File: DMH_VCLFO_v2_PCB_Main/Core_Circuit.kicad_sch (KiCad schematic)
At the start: 70 parts, among them J12 Conn_02x06_Top_Bottom, J13 Conn_02x03_Top_Bottom, J14 Conn_02x03_Top_Bottom, J15 Conn_02x06_Top_Bottom, J16 Conn_02x03_Top_Bottom, Q10 BC558, Q11 MMBFJ113, Q3 MMBFJ113, Q5 BC548, Q7 BC548, Q8 BC548, Q9 BC558, U3 TL074, U4 TL074, U5 TL074, U6 TL074

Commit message: Replaced sine shaper and adapted random
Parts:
- added C4: 1uF, Capacitor_THT:C_Disc_D4.3mm_W1.9mm_P5.00mm, symbol Device:C
- added C5: 1nF, Capacitor_THT:C_Disc_D4.3mm_W1.9mm_P5.00mm, symbol Device:C
- added C8: 100nF, Capacitor_THT:C_Disc_D4.3mm_W1.9mm_P5.00mm, symbol Device:C
- added D8, D9: 1N4148, Diode_THT:D_DO-35_SOD27_P7.62mm_Horizontal, symbol Device:D
- added Q12, Q13, Q4: BC548, Package_TO_SOT_THT:TO-92_Inline_Wide, symbol Transistor_BJT:BC548
- added Q6: J113, Package_TO_SOT_THT:TO-92L_Inline, symbol Transistor_FET:MMBFJ113
- added R100, R101: 14k, Resistor_THT:R_Axial_DIN0207_L6.3mm_D2.5mm_P7.62mm_Horizontal, symbol Device:R_US
- added R102: 1k, Resistor_THT:R_Axial_DIN0207_L6.3mm_D2.5mm_P7.62mm_Horizontal, symbol Device:R_US
- added R47, R50, R55, R58, R60: 100k, Resistor_THT:R_Axial_DIN0207_L6.3mm_D2.5mm_P7.62mm_Horizontal, symbol Device:R_US
- added R51, R92, R96: 10k, Resistor_THT:R_Axial_DIN0207_L6.3mm_D2.5mm_P7.62mm_Horizontal, symbol Device:R_US
- added R54: 330R, Resistor_THT:R_Axial_DIN0207_L6.3mm_D2.5mm_P7.62mm_Horizontal, symbol Device:R_US
- added R57: 33k, Resistor_THT:R_Axial_DIN0207_L6.3mm_D2.5mm_P7.62mm_Horizontal, symbol Device:R_US
- added R61: 1M, Resistor_THT:R_Axial_DIN0207_L6.3mm_D2.5mm_P7.62mm_Horizontal, symbol Device:R_US
- added R91, R97: 2k2, Resistor_THT:R_Axial_DIN0207_L6.3mm_D2.5mm_P7.62mm_Horizontal, symbol Device:R_US
- added R94: 390, Resistor_THT:R_Axial_DIN0207_L6.3mm_D2.5mm_P7.62mm_Horizontal, symbol Device:R_US
- added R95: 18k, Resistor_THT:R_Axial_DIN0207_L6.3mm_D2.5mm_P7.62mm_Horizontal, symbol Device:R_US
- added RV10: 50k, Potentiometer_THT:Potentiometer_Bourns_3296W_Vertical, symbol Device:R_Potentiometer_Trim_US
- added RV9: 100k, Potentiometer_THT:Potentiometer_Bourns_3296W_Vertical, symbol Device:R_Potentiometer_Trim_US
- added unit 1 of U3
- added unit 4 of U3
- added unit 2 of U3
- added unit 1 of U6
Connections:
- net Rmp is gone; now on net A_Rmp_S: R77.2, U4.14
- net +12V: now also R47.1, R60.1, R92.1, R96.1
- net -12V: now also R95.1
- net A_CV_M: now also J16.4 (Pin_4); no longer J16.5 (Pin_5)
- net A_CV_S: now also J13.4 (Pin_4); no longer J13.5 (Pin_5)
- net A_Freq_Pot_p2_M: now also J15.3 (Pin_3); no longer R99.2
- net A_Sync_M: now also J16.1 (Pin_1); no longer J16.2 (Pin_2)
- net A_Sync_S: now also J13.1 (Pin_1); no longer J13.2 (Pin_2)
- net A_Tri_S: now also RV9.1, RV9.2
- net GND: now also C8.2, Q4.2 (B), R100.2, R50.2, R51.2, R54.2, R55.2, R57.2, R91.2, R97.2
- net Sqr_Raw: now also D8.2 (A)
- net A_Rnd_M: now reaches J15.10 (Pin_10)
- net A_Rmp_M: now reaches J15.4 (Pin_4)
- net A_Rnd_S: now reaches J12.10 (Pin_10)
- net A_Rnd_S: now also U3.6 (-), U3.7
- net A_Freq_Pot_p2_S: now reaches J12.3 (Pin_3)
- net A_Freq_Pot_p2_S: now also R99.2
- net A_Rmp_S: now reaches J12.4 (Pin_4)
- net Saw renamed A_Saw_S
- net A_Saw_S: now also J13.2 (Pin_2)
- new net: D9.1 (K), U3.14
- new net: D9.2 (A), Q6.3 (G), R61.2
- new net: Q6.1 (D), R58.1, R61.1, U3.1
- new net: R54.1, R58.2, U3.2 (-)
- new net: R101.2, R102.2, U6.1
- new net: C4.2, R50.1, U3.3 (+)
- new net: Q13.3 (E), R94.2, RV10.1
- new net: R95.2, RV10.2
- new net: Q12.3 (E), R94.1, RV10.3
- new net: Q12.1 (C), R101.1, R92.2, U6.2 (-)
- new net: R57.1, R60.2, U3.13 (-)
- new net: Q12.2 (B), R91.1, RV9.3
- new net: Q13.1 (C), R100.1, R96.2, U6.3 (+)
- new net: Q13.2 (B), R97.1
- new net: C4.1, Q4.3 (E), R47.2
- new net: C5.1, R55.1, U3.12 (+)
- new net: C5.2, D8.1 (K), R51.1
- new net: C8.1, Q6.2 (S), U3.5 (+)
- new net A_Saw_M: J16.2 (Pin_2)
- new net A_Sin_M: J16.5 (Pin_5)
- new net A_Sin_S: J13.5 (Pin_5), R102.1
- no-connect marks 0 -> 1

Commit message: Improved inter-PCB connections
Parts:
- removed J12: Conn_02x06_Top_Bottom, Connector_PinHeader_2.54mm:PinHeader_2x06_P2.54mm_Horizontal, symbol Connector_Generic:Conn_02x06_Top_Bottom
- removed J15: Conn_02x06_Top_Bottom, Connector_PinSocket_2.54mm:PinSocket_2x06_P2.54mm_Vertical, symbol Connector_Generic:Conn_02x06_Top_Bottom
- removed R40: 1k, Resistor_THT:R_Axial_DIN0207_L6.3mm_D2.5mm_P7.62mm_Horizontal, symbol Device:R_US
- added C21, C22: 100nF, Capacitor_THT:C_Disc_D4.3mm_W1.9mm_P5.00mm, symbol Device:C
- added J12, J120: Conn_02x03_Odd_Even, Connector_PinHeader_2.54mm:PinHeader_2x03_P2.54mm_Horizontal, symbol Connector_Generic:Conn_02x03_Odd_Even
- added unit 5 of U12
- J11: renamed from J14; value Conn_02x03_Top_Bottom -> Conn_02x03_Odd_Even; symbol Connector_Generic:Conn_02x03_Top_Bottom -> Connector_Generic:Conn_02x03_Odd_Even
- J110, J130: renamed from J13; value Conn_02x03_Top_Bottom -> Conn_02x03_Odd_Even; symbol Connector_Generic:Conn_02x03_Top_Bottom -> Connector_Generic:Conn_02x03_Odd_Even
- J13: renamed from J16; value Conn_02x03_Top_Bottom -> Conn_02x03_Odd_Even; symbol Connector_Generic:Conn_02x03_Top_Bottom -> Connector_Generic:Conn_02x03_Odd_Even
- R77: renamed from R74; value 10k -> 100k
- R79: renamed from R77; value 10k -> 100k
- renumbered C5 to C10, C14 to C11, C9 to C12, C7 to C13, C7 to C14, C6 to C15, C12 to C17, C13 to C18, C14 to C19, C15 to C20, C3 to C5, C11 to C6, C4 to C7, C15 to C9, D9 to D10, D8 to D11, D10 to D12, D17 to D7, D18 to D8, D7 to D9, Q5 to Q10, Q8 to Q11, Q9 to Q12, Q10 to Q13, Q7 to Q14, Q3 to Q15, Q11 to Q16, Q12 to Q17, Q13 to Q18, Q4 to Q19, Q6 to Q20, R85 to R37, R81 to R38, R101 to R39, R86 to R40, R92 to R43, R96 to R44, R39 to R45, R80 to R46, R79 to R47, R102 to R48, R82 to R49, R49 to R50, R44 to R51, R83 to R52, R91 to R53, R97 to R54, R100 to R55, R94 to R56, R99 to R57, R95 to R58, R38 to R59, R47 to R60, R37 to R61, R58 to R62, R50 to R63, R54 to R64, R61 to R65, R52 to R66, R56 to R67, R87 to R68, R88 to R69, R51 to R70, R55 to R71, R59 to R72, R57 to R74, R60 to R75, R68 to R76, R89 to R80, R90 to R81, R93 to R82, R64 to R83, R46 to R84, R65 to R85, R45 to R86, R62 to R87, R48 to R88, R43 to R89, R53 to R90, R72 to R91, R84 to R92, RV9 to RV4, RV10 to RV5, U6 to U10, U5 to U10, U4 to U11, U5 to U11, U3 to U11, U6 to U11, U3 to U12, U6 to U12
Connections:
- net +12V: now also J11.3 (Pin_3), J11.4 (Pin_4), J110.3 (Pin_3), J110.4 (Pin_4), C21.1, U12.4 (V+); no longer J11.1 (Pin_1), J110.1 (Pin_1)
- net -12V: now also J11.5 (Pin_5), J11.6 (Pin_6), J110.5 (Pin_5), J110.6 (Pin_6), C22.2, U12.11 (V-); no longer J11.3 (Pin_3), J11.4 (Pin_4), J110.3 (Pin_3), J110.4 (Pin_4)
- net A_CV_M: now also J12.3 (Pin_3); no longer J13.4 (Pin_4)
- net A_CV_S: now also J120.3 (Pin_3); no longer J130.4 (Pin_4)
- net A_Freq_Pot_p2_M: now also J12.1 (Pin_1)
- net A_Freq_Pot_p2_S: now also J120.1 (Pin_1)
- net A_Rmp_M: now also J13.1 (Pin_1)
- net A_Rmp_S: now also J130.1 (Pin_1), U11.7; no longer U11.14
- net A_Rnd_M: now also J13.2 (Pin_2)
- net A_Rnd_S: now also J130.2 (Pin_2)
- net A_Rng_Sw_p1_M: now also J12.2 (Pin_2)
- net A_Rng_Sw_p1_S: now also J120.2 (Pin_2)
- net A_Rng_Sw_p3_M: now also J12.4 (Pin_4)
- net A_Rng_Sw_p3_S: now also J120.4 (Pin_4)
- net A_Saw_M: now also J13.3 (Pin_3); no longer J13.2 (Pin_2)
- net A_Saw_S: now also J130.3 (Pin_3); no longer J130.2 (Pin_2)
- net A_Sin_M: now also J13.4 (Pin_4); no longer J13.5 (Pin_5)
- net A_Sin_S: now also J130.4 (Pin_4); no longer J130.5 (Pin_5)
- net A_Sqr_M: now also J13.5 (Pin_5); no longer J13.3 (Pin_3)
- net A_Sqr_S: now also J130.5 (Pin_5); no longer J130.3 (Pin_3)
- net A_Sync_M: now also J12.5 (Pin_5); no longer J13.1 (Pin_1)
- net A_Sync_S: now also J120.5 (Pin_5); no longer J130.1 (Pin_1)
- net A_Tri_S: now also C14.1, U10.9 (-)
- net GND: now also J11.1 (Pin_1), J11.2 (Pin_2), J110.1 (Pin_1), J110.2 (Pin_2), U11.5 (+), C21.2, C22.1, J12.6 (Pin_6), J120.6 (Pin_6); no longer J11.5 (Pin_5), J11.6 (Pin_6), J110.5 (Pin_5), J110.6 (Pin_6), U11.12 (+)
- net at R77.2, R79.1: now also U11.6 (-); no longer U11.13 (-)
- net at R39.2, R48.2: now also U12.8; no longer U12.1
- net at Q17.1 (C), R39.1, R43.2: now also U12.9 (-); no longer U12.2 (-)
- net at Q18.1 (C), R44.2, R55.1: now also U12.10 (+); no longer U12.3 (+)
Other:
- note removed: "Check if this 1k can be removed"
- moved on the sheet: C17, C18, C19, C20, U10E, U11E

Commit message: Notes from breadboarding
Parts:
- removed R51, R75: 100k, Resistor_THT:R_Axial_DIN0207_L6.3mm_D2.5mm_P7.62mm_Horizontal, symbol Device:R_US
- removed R74: 33k, Resistor_THT:R_Axial_DIN0207_L6.3mm_D2.5mm_P7.62mm_Horizontal, symbol Device:R_US
- Q17, Q18, Q19: footprint Package_TO_SOT_THT:TO-92_Inline_Wide -> Package_TO_SOT_THT:TO-92L_Inline_Wide
- R37, R47: value 22k -> 18k
- R49, R50: value 100k -> 47k
- R63: value 100k -> 14k
- U11: footprint (none) -> Package_DIP:DIP-14_W7.62mm_Socket
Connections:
- net GND: no longer R50.2
- net at C6.2, R52.1, U11.9 (-): now also R50.2; no longer R49.2
- net Comp_Ref: now reaches R50.1, U11.13 (-)
- net Comp_Ref: now also R49.2, U12.13 (-)
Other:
- note added: "2k in bb"
- moved on the sheet: C6, R49, R50, R52

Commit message: Sch redesign in progress
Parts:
- removed R48: 1k, Resistor_THT:R_Axial_DIN0207_L6.3mm_D2.5mm_P7.62mm_Horizontal, symbol Device:R_US
- added R8: 1k, Resistor_THT:R_Axial_DIN0207_L6.3mm_D2.5mm_P7.62mm_Horizontal, symbol Device:R_US
- added R9: 100k, Resistor_THT:R_Axial_DIN0207_L6.3mm_D2.5mm_P7.62mm_Horizontal, symbol Device:R_US
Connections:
- net A_Sin_S: now also R8.2
- net GND: no longer J12.6 (Pin_6), J120.6 (Pin_6)
- net at R39.2, U12.8: now also R8.1
- net at R57.1, R59.1, R61.1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: now also R9.1
- new net A_Bus_CV_M: J12.6 (Pin_6)
- new net A_Bus_CV_S: J120.6 (Pin_6), R9.2

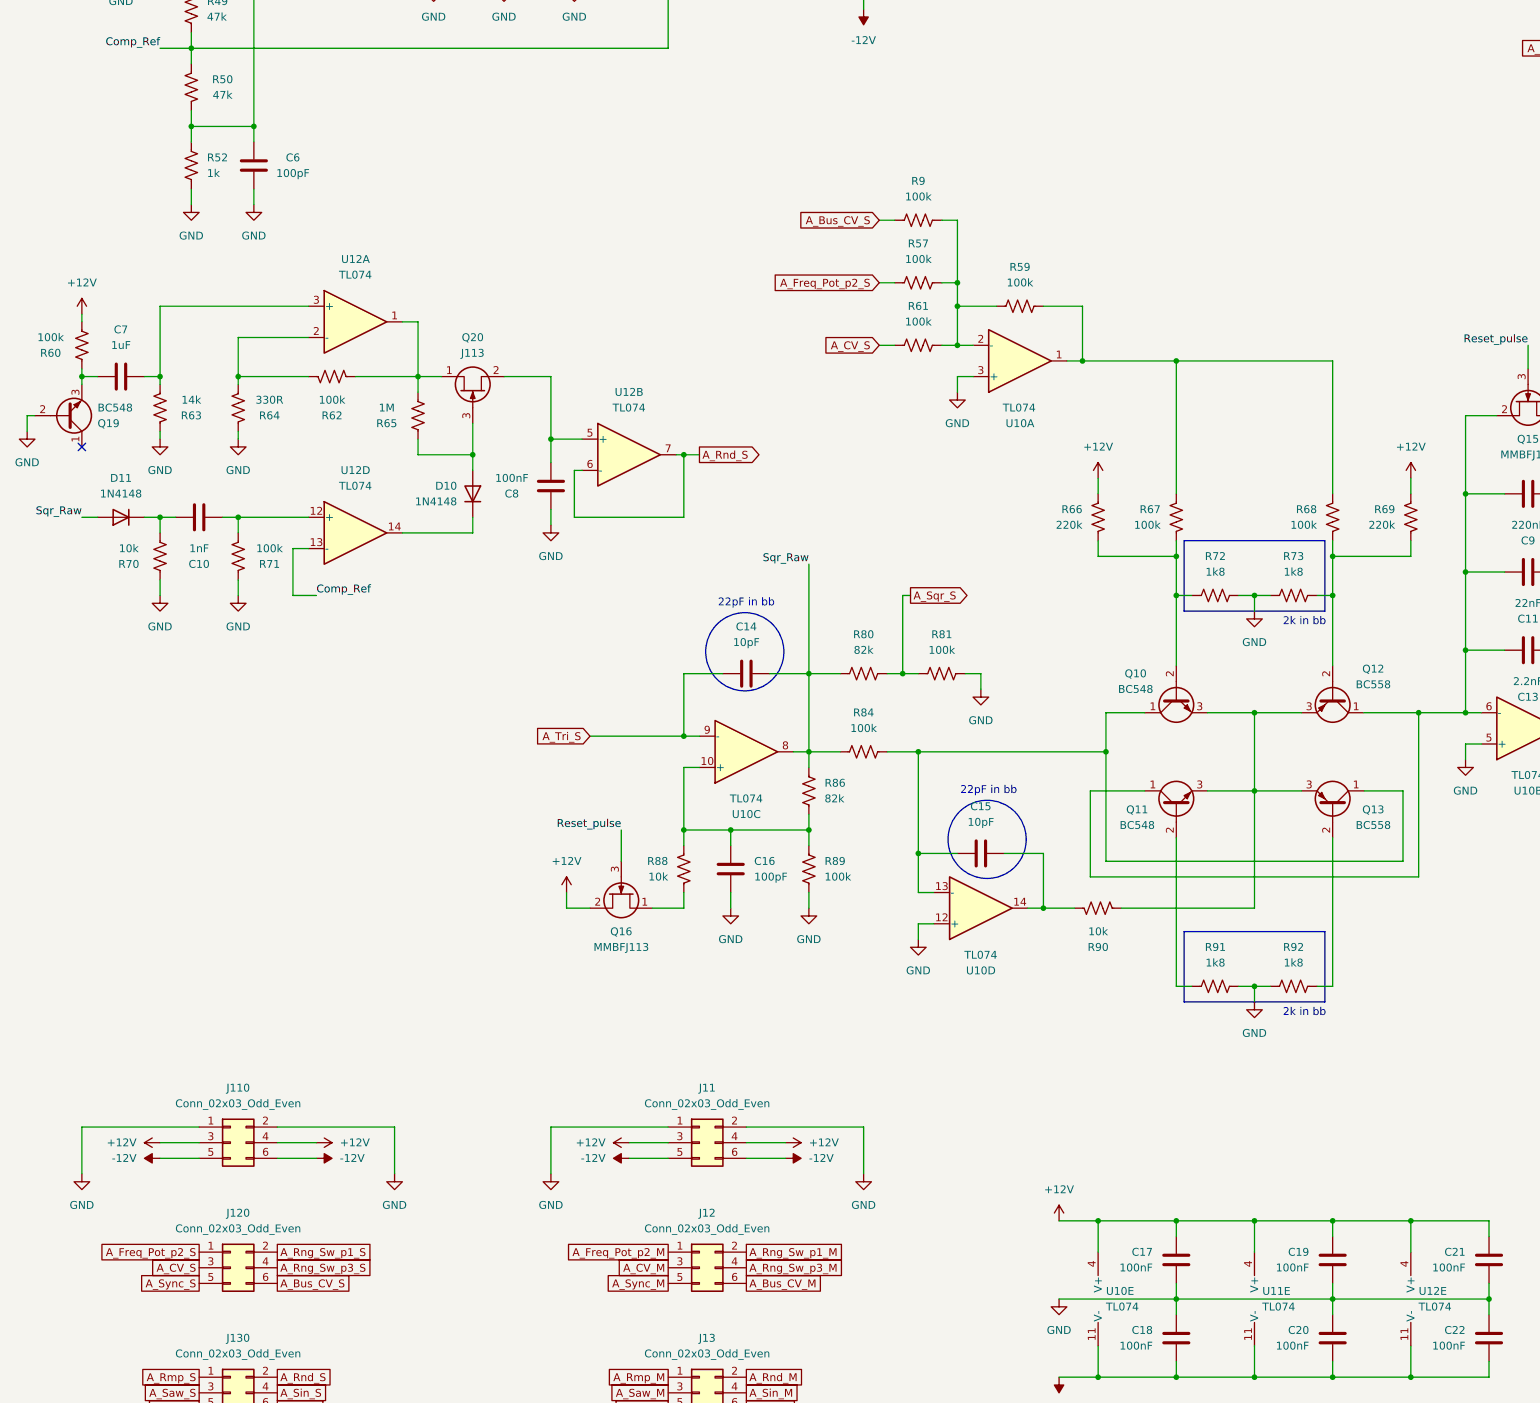
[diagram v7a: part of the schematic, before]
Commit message: Redesigned schematic for V/Oct
And also Bus CV and Fine tune
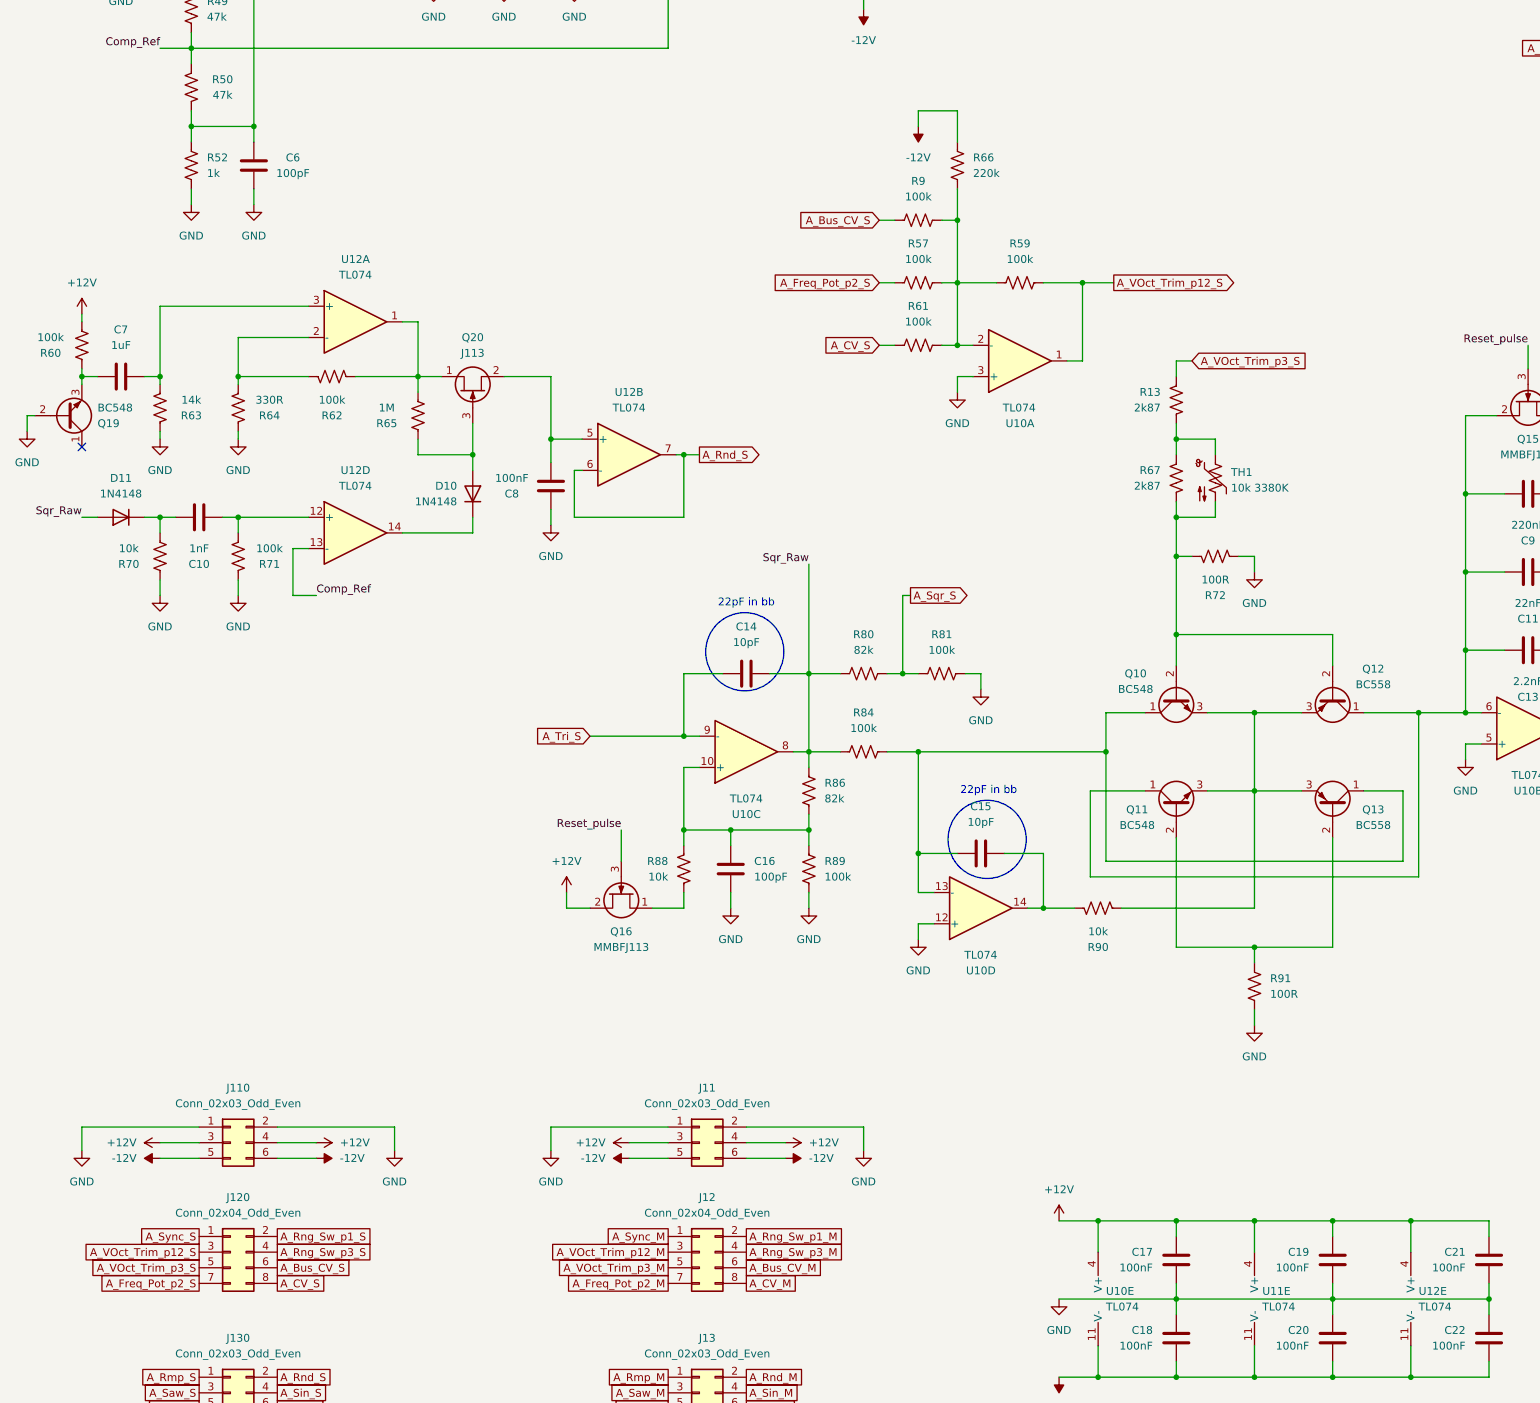
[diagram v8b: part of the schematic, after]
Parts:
- removed R68: 100k, Resistor_THT:R_Axial_DIN0207_L6.3mm_D2.5mm_P7.62mm_Horizontal, symbol Device:R_US
- removed R69: 220k, Resistor_THT:R_Axial_DIN0207_L6.3mm_D2.5mm_P7.62mm_Horizontal, symbol Device:R_US
- removed R73, R92: 1k8, Resistor_THT:R_Axial_DIN0207_L6.3mm_D2.5mm_P7.62mm_Horizontal, symbol Device:R_US
- added R13: 2k87, Resistor_THT:R_Axial_DIN0207_L6.3mm_D2.5mm_P7.62mm_Horizontal, symbol Device:R_US
- added TH1: 10k 3380K, Resistor_THT:R_Axial_DIN0204_L3.6mm_D1.6mm_P1.90mm_Vertical, symbol Device:Thermistor_NTC_US
- J12, J120: value Conn_02x03_Odd_Even -> Conn_02x04_Odd_Even; footprint Connector_PinHeader_2.54mm:PinHeader_2x03_P2.54mm_Horizontal -> Connector_PinHeader_2.54mm:PinHeader_2x04_P2.54mm_Horizontal; symbol Connector_Generic:Conn_02x03_Odd_Even -> Connector_Generic:Conn_02x04_Odd_Even
- R67: value 100k -> 2k87
- R72, R91: value 1k8 -> 100R
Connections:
- net +12V: no longer R66.1
- net -12V: now also R66.1
- net A_CV_M: now also J12.8 (Pin_8); no longer J12.3 (Pin_3)
- net A_CV_S: now also J120.8 (Pin_8); no longer J120.3 (Pin_3)
- net A_Freq_Pot_p2_M: now also J12.7 (Pin_7); no longer J12.1 (Pin_1)
- net A_Freq_Pot_p2_S: now also J120.7 (Pin_7); no longer J120.1 (Pin_1)
- net A_Sync_M: now also J12.1 (Pin_1); no longer J12.5 (Pin_5)
- net A_Sync_S: now also J120.1 (Pin_1); no longer J120.5 (Pin_5)
- net GND: now also R91.2; no longer R91.1
- net at Q13.2 (B): now also Q11.2 (B), R91.1
- net A_VOct_Trim_p12_S: now reaches R59.2, U10.1
- net A_VOct_Trim_p12_S: now also J120.3 (Pin_3); no longer R67.1
- net at Q10.2 (B), R67.2, R72.2: now also Q12.2 (B), TH1.2; no longer R66.2
- net at R57.1, R59.1, R61.1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: now also R66.2
- new net: R13.2, R67.1, TH1.1
- new net A_VOct_Trim_p12_M: J12.3 (Pin_3)
- new net A_VOct_Trim_p3_M: J12.5 (Pin_5)
- new net A_VOct_Trim_p3_S: J120.5 (Pin_5), R13.1
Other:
- moved on the sheet: R59, R66, R67, R72, R91
